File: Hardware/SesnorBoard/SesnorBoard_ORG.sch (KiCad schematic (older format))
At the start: 31 parts, among them J1 Mainboard connection, J2 microphoon connection, U1 AMG8833, U2 CCS811, U3 NC7SVU04P5X

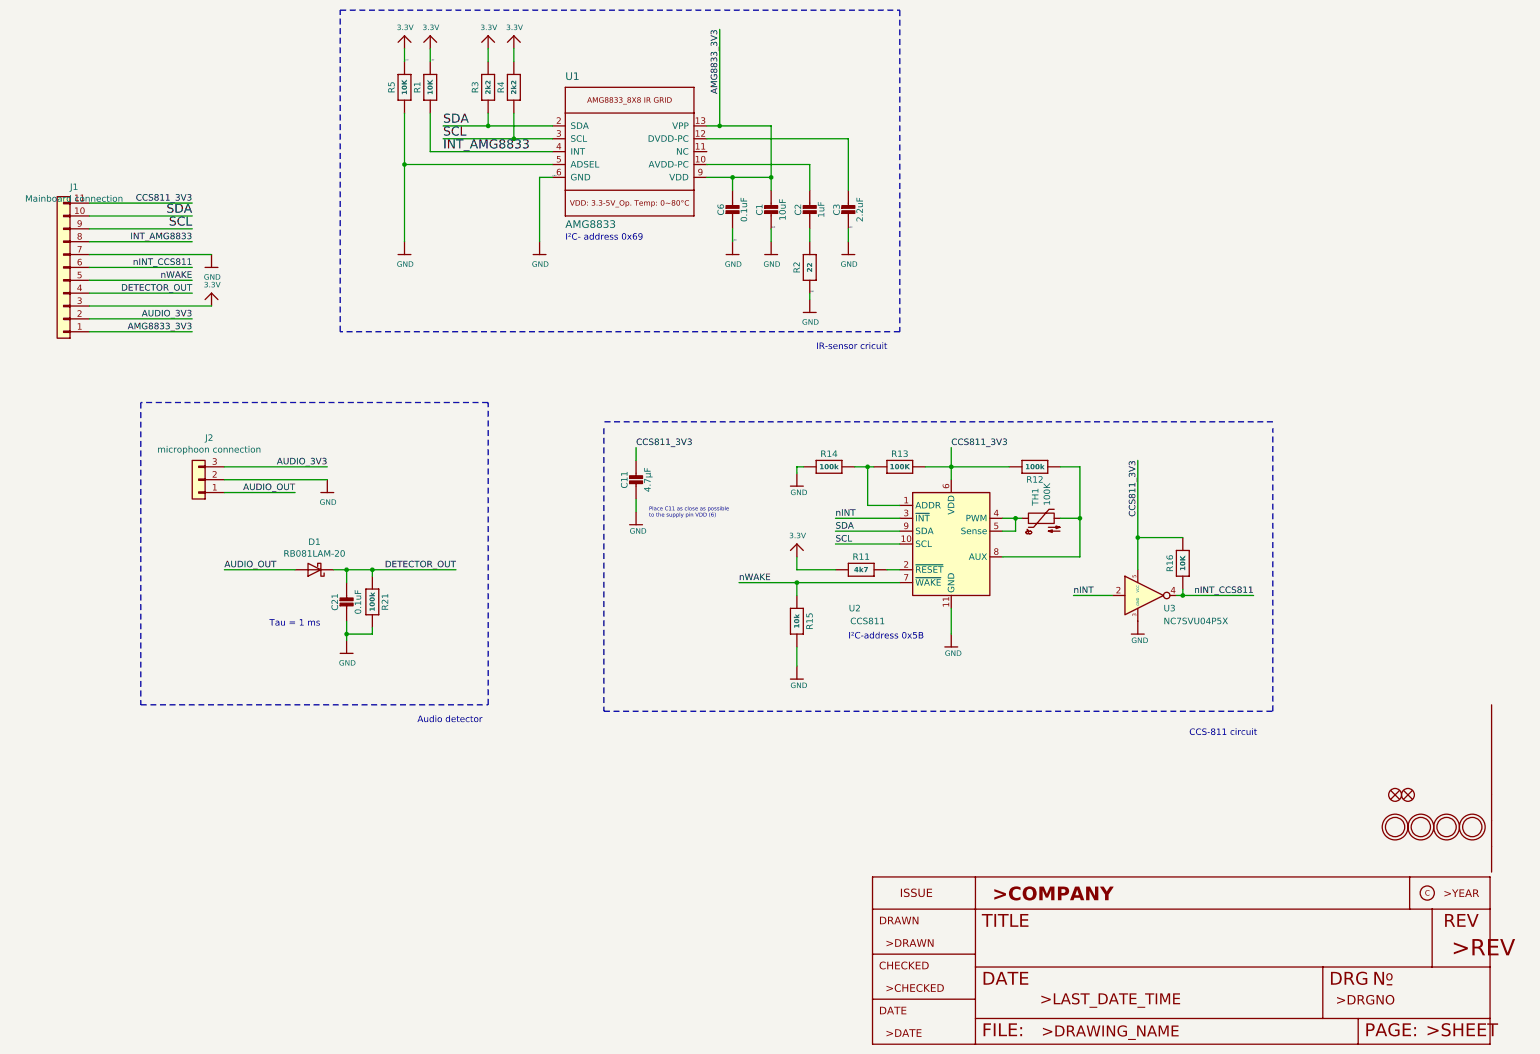
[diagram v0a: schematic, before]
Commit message: Figures added sensor part in report
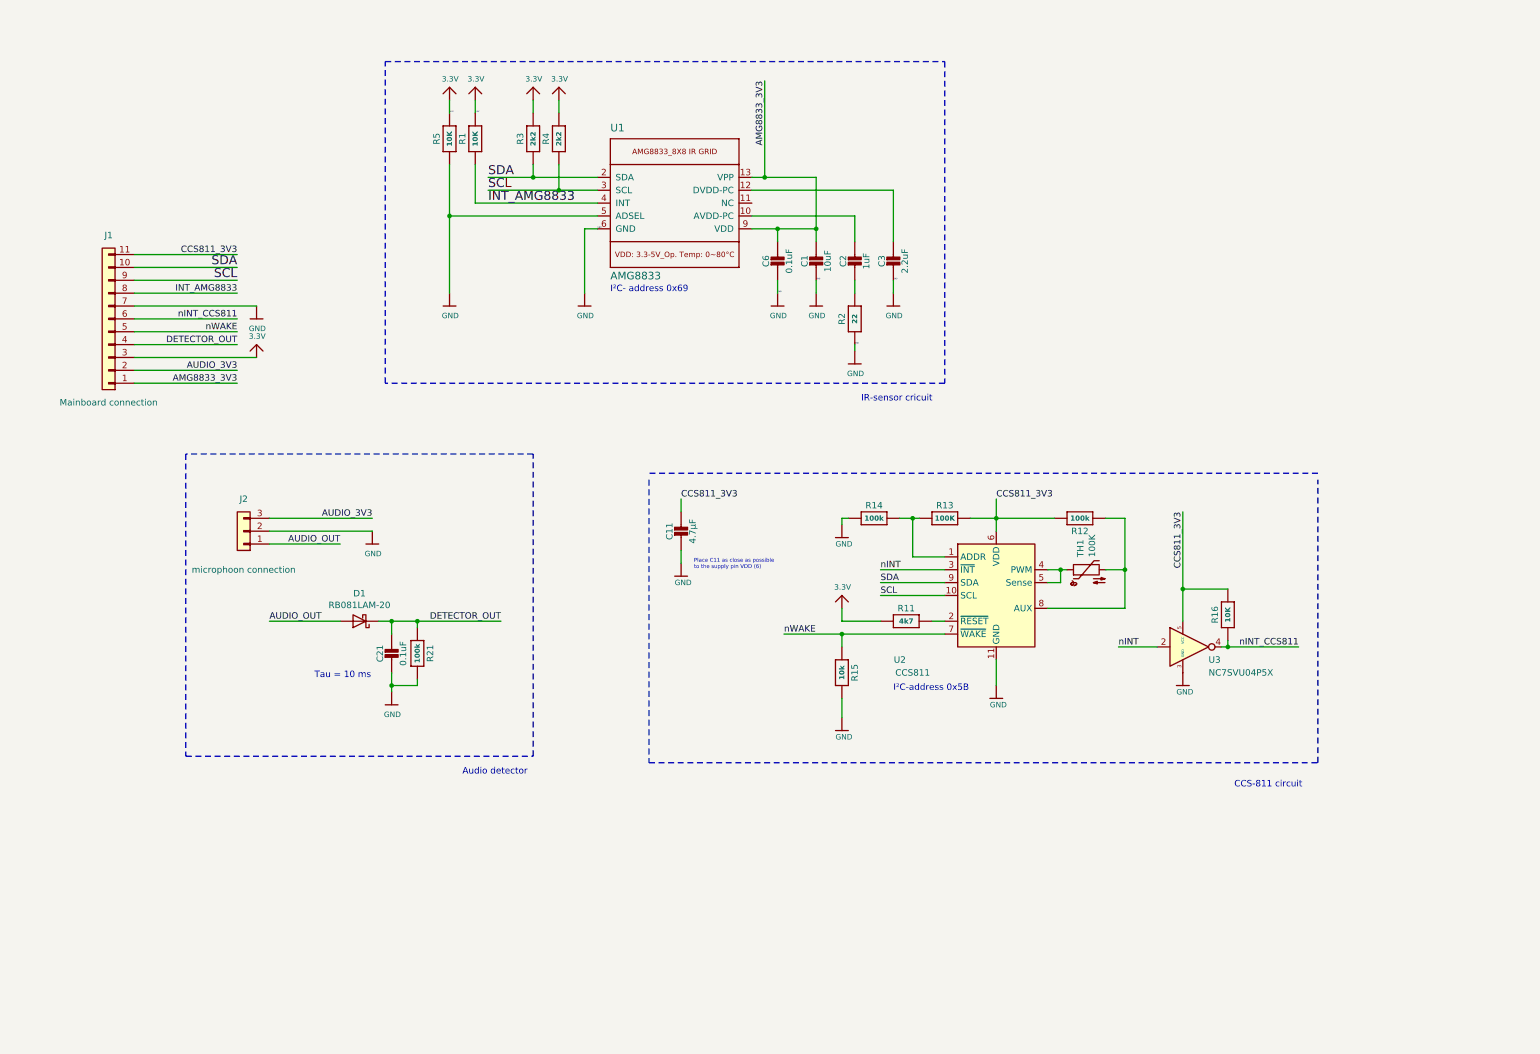
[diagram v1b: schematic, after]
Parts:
- removed FID2, FID3: FIDUCIAL_1MM, SesnorBoard:FIDUCIAL_1MM, symbol SesnorBoard-eagle-import:FIDUCIAL_1MM
- removed U$16, U$17, U$18, U$19: MOUNTINGHOLE2.5, SesnorBoard:MOUNTINGHOLE_2.5_PLATED, symbol SesnorBoard-eagle-import:MOUNTINGHOLE2.5
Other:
- note added: "Tau = 10 ms"
- note removed: "Tau = 1 ms"
- moved on the sheet: C1, C11, C2, C21, C3, C6, D1, J1, J2, R1, R11, R12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
